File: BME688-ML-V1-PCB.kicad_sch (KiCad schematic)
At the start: 32 parts, among them SW1 434133025816, U1 STM32L431KBU6TR, U2 BME688, U3 BME688

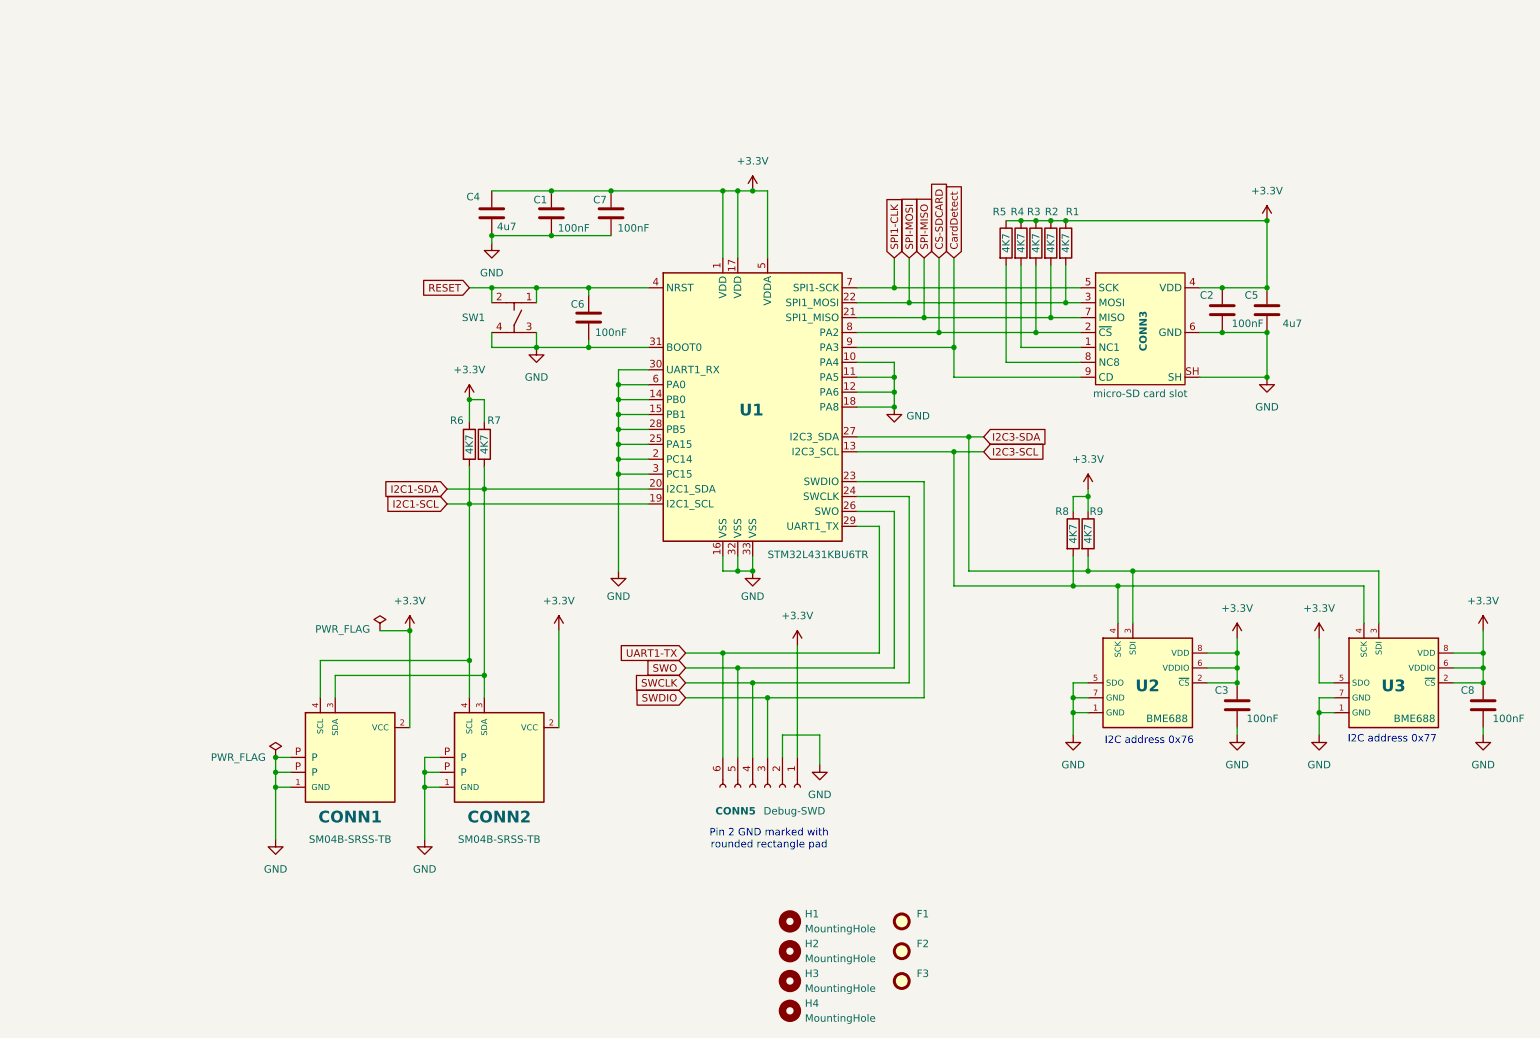
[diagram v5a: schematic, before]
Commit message: Add #3 and fix #5
Add application button
Add RGB led
Move SD-card connector to align inserted card with PCB edge
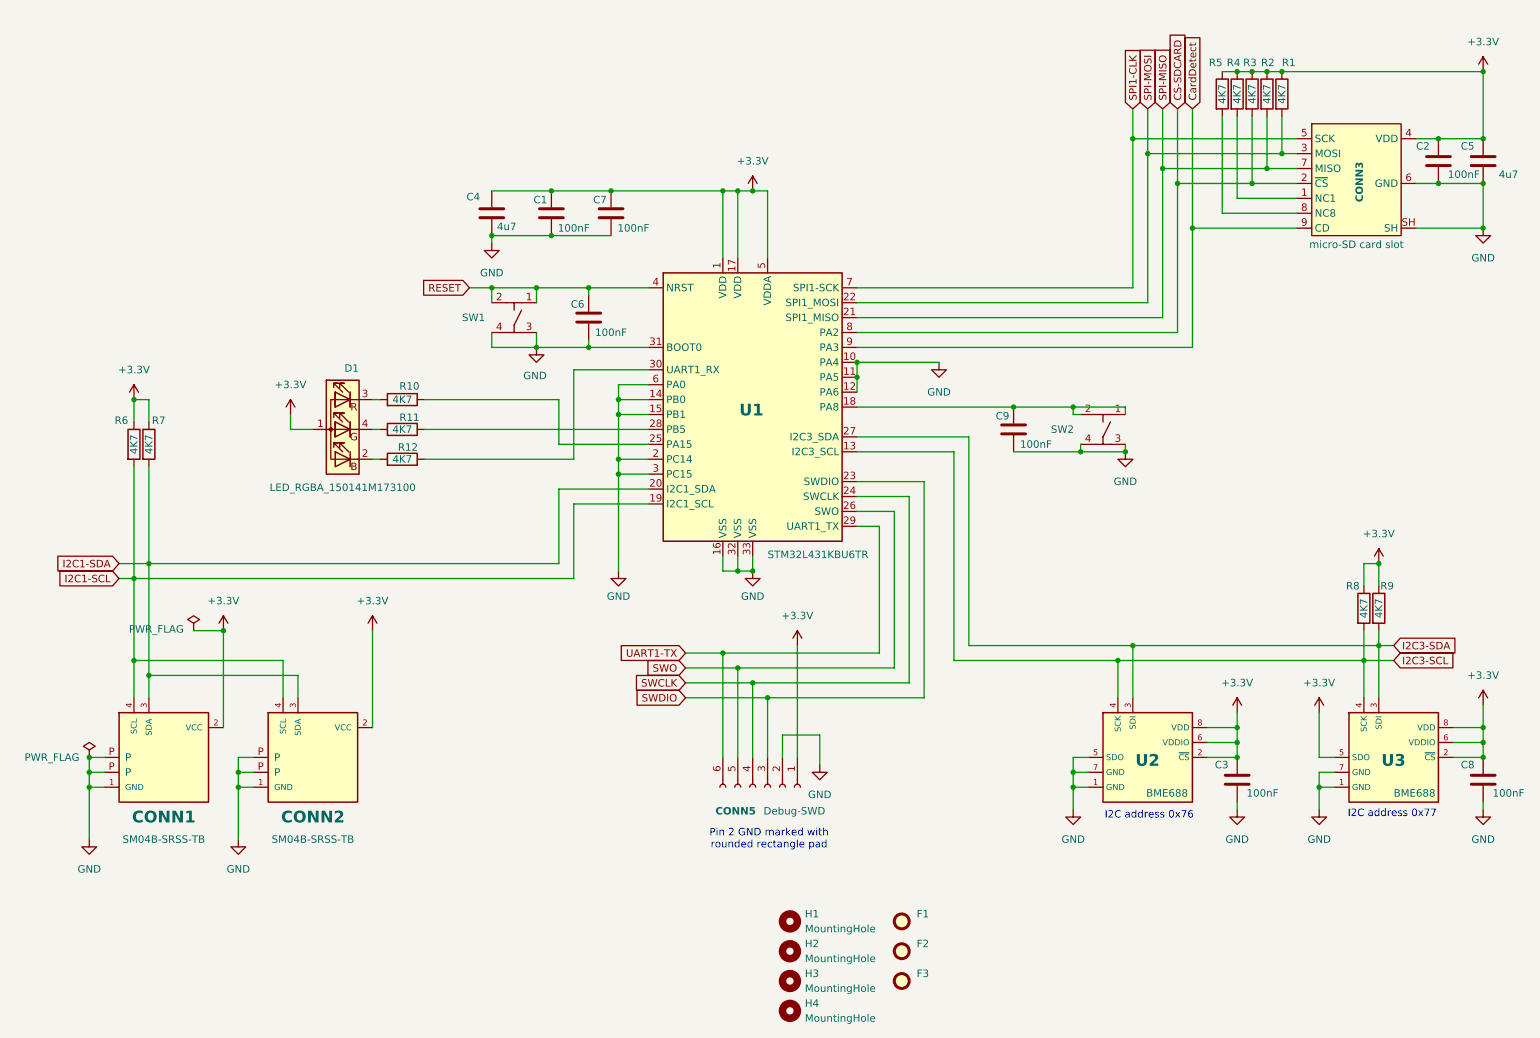
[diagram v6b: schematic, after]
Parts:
- added C9: KGM15AR71C104KT, 1projectLibrary:C_0603_nominal, symbol Device:C
- added D1: LED_RGBA_150141M173100, 1projectLibrary:RGB_LED_150141M173100, symbol 1projectLibrary:LED_RGBA_150141M173100
- added R10, R11, R12: CR0603-FX-4701ELF, 1projectLibrary:R_0603_nominal, symbol Device:R
- added SW2: 434133025816, 1projectLibrary:Wurth-434133025816, symbol 1projectLibrary:Switch_434133025816
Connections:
- net +3.3V: now also D1.1 (A)
- net GND: now also C9.2, SW2.3, SW2.4; no longer U1.18 (PA8), U1.25 (PA15), U1.28 (PB5), U1.30 (UART1_RX)
- new net: R10.1, U1.25 (PA15)
- new net: D1.3 (RK), R10.2
- new net: C9.1, SW2.1, SW2.2, U1.18 (PA8)
- new net: R11.1, U1.28 (PB5)
- new net: R12.1, U1.30 (UART1_RX)
- new net: D1.2 (BK), R12.2
- new net: D1.4 (GK), R11.2
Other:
- moved on the sheet: C2, C3, C5, C8, CONN1, CONN2, CONN3, R1, R2, R3, R4, R5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
